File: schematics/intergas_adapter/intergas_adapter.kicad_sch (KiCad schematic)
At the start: 12 parts, among them J1 RJ45, Q1 BC337, Q2 BC337, U1 4N25, U2 ESP-12E, U3 4N25, U4 HT7533-1-TO92

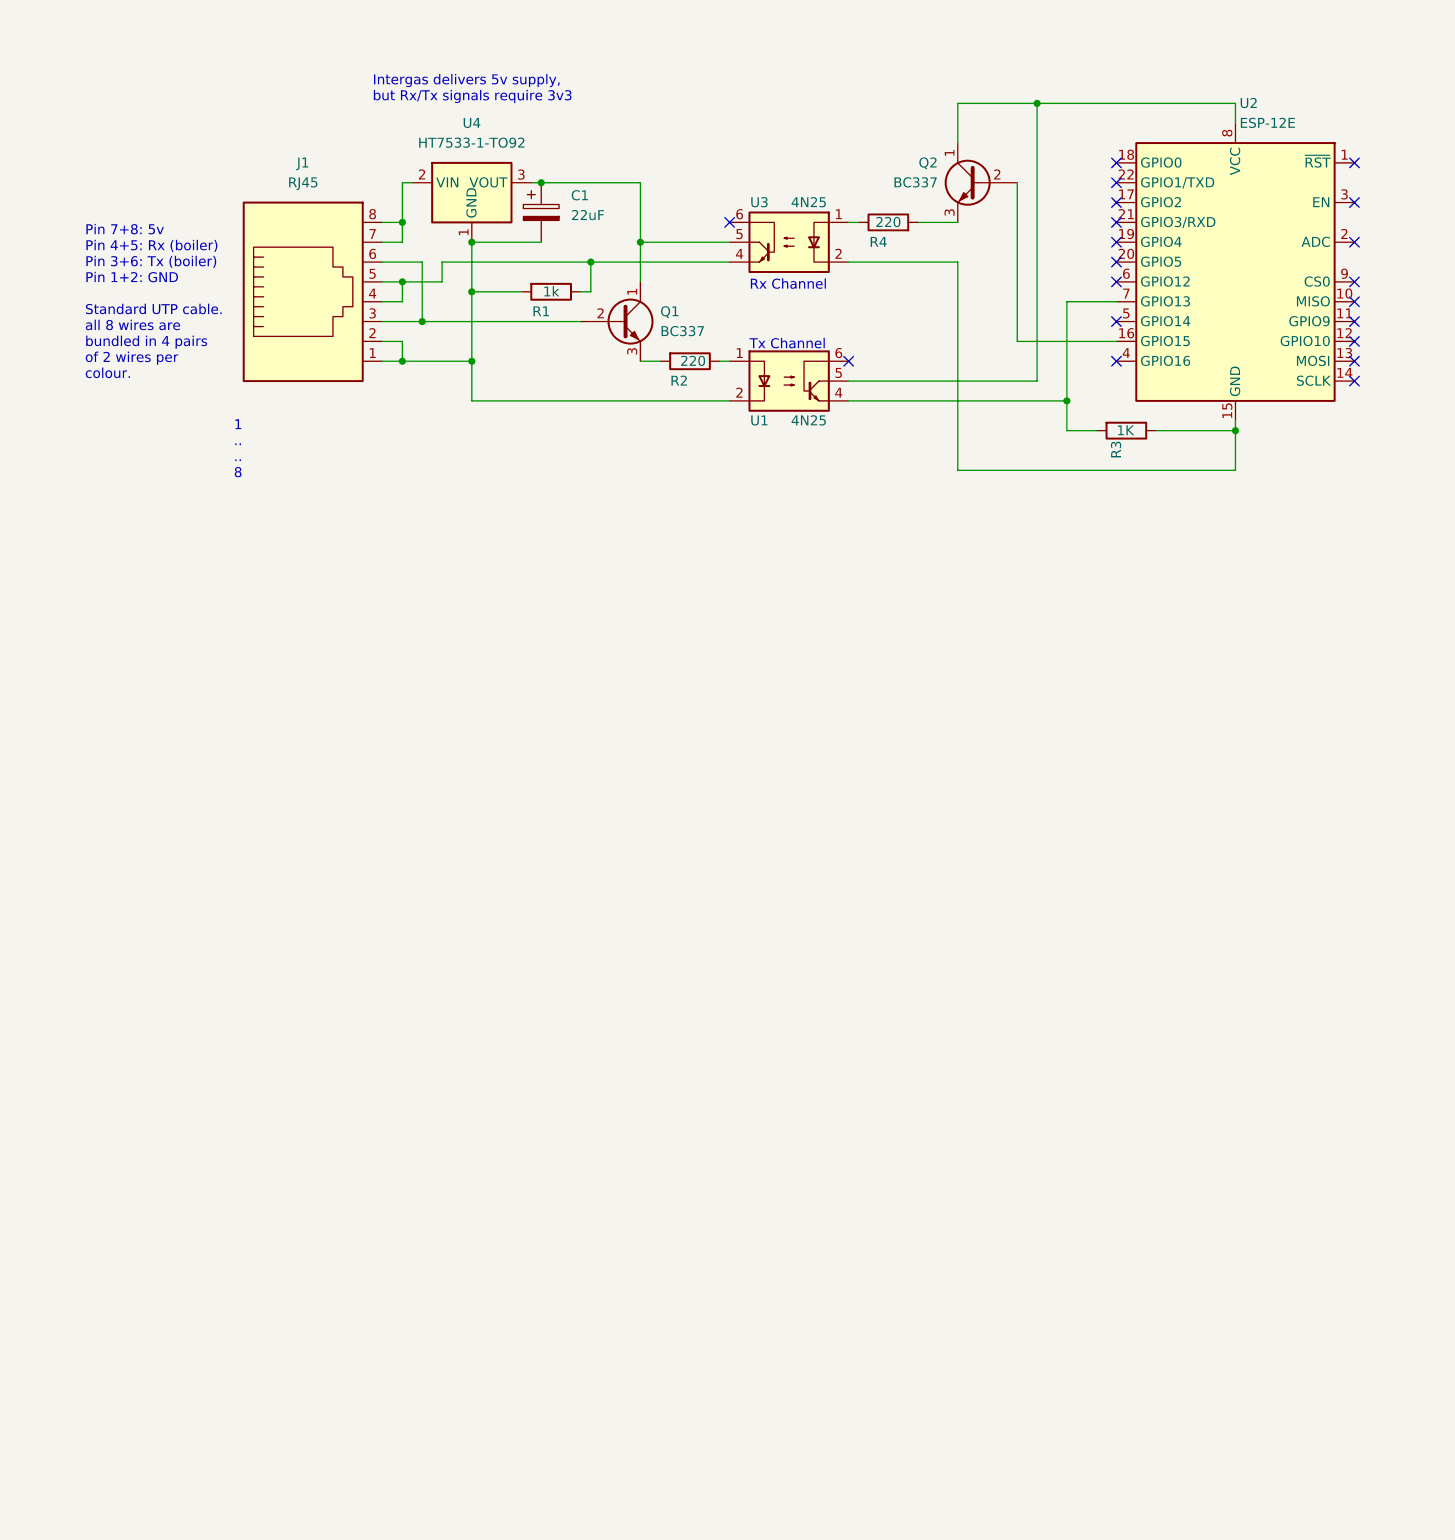
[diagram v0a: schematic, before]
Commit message: Add NodeMCU-ESP32 support
Next to the NodeMCU-ESP8266 we do now support also a
NodeMCU-ESP32 board: https://esphome.io/devices/nodemcu_esp32.html
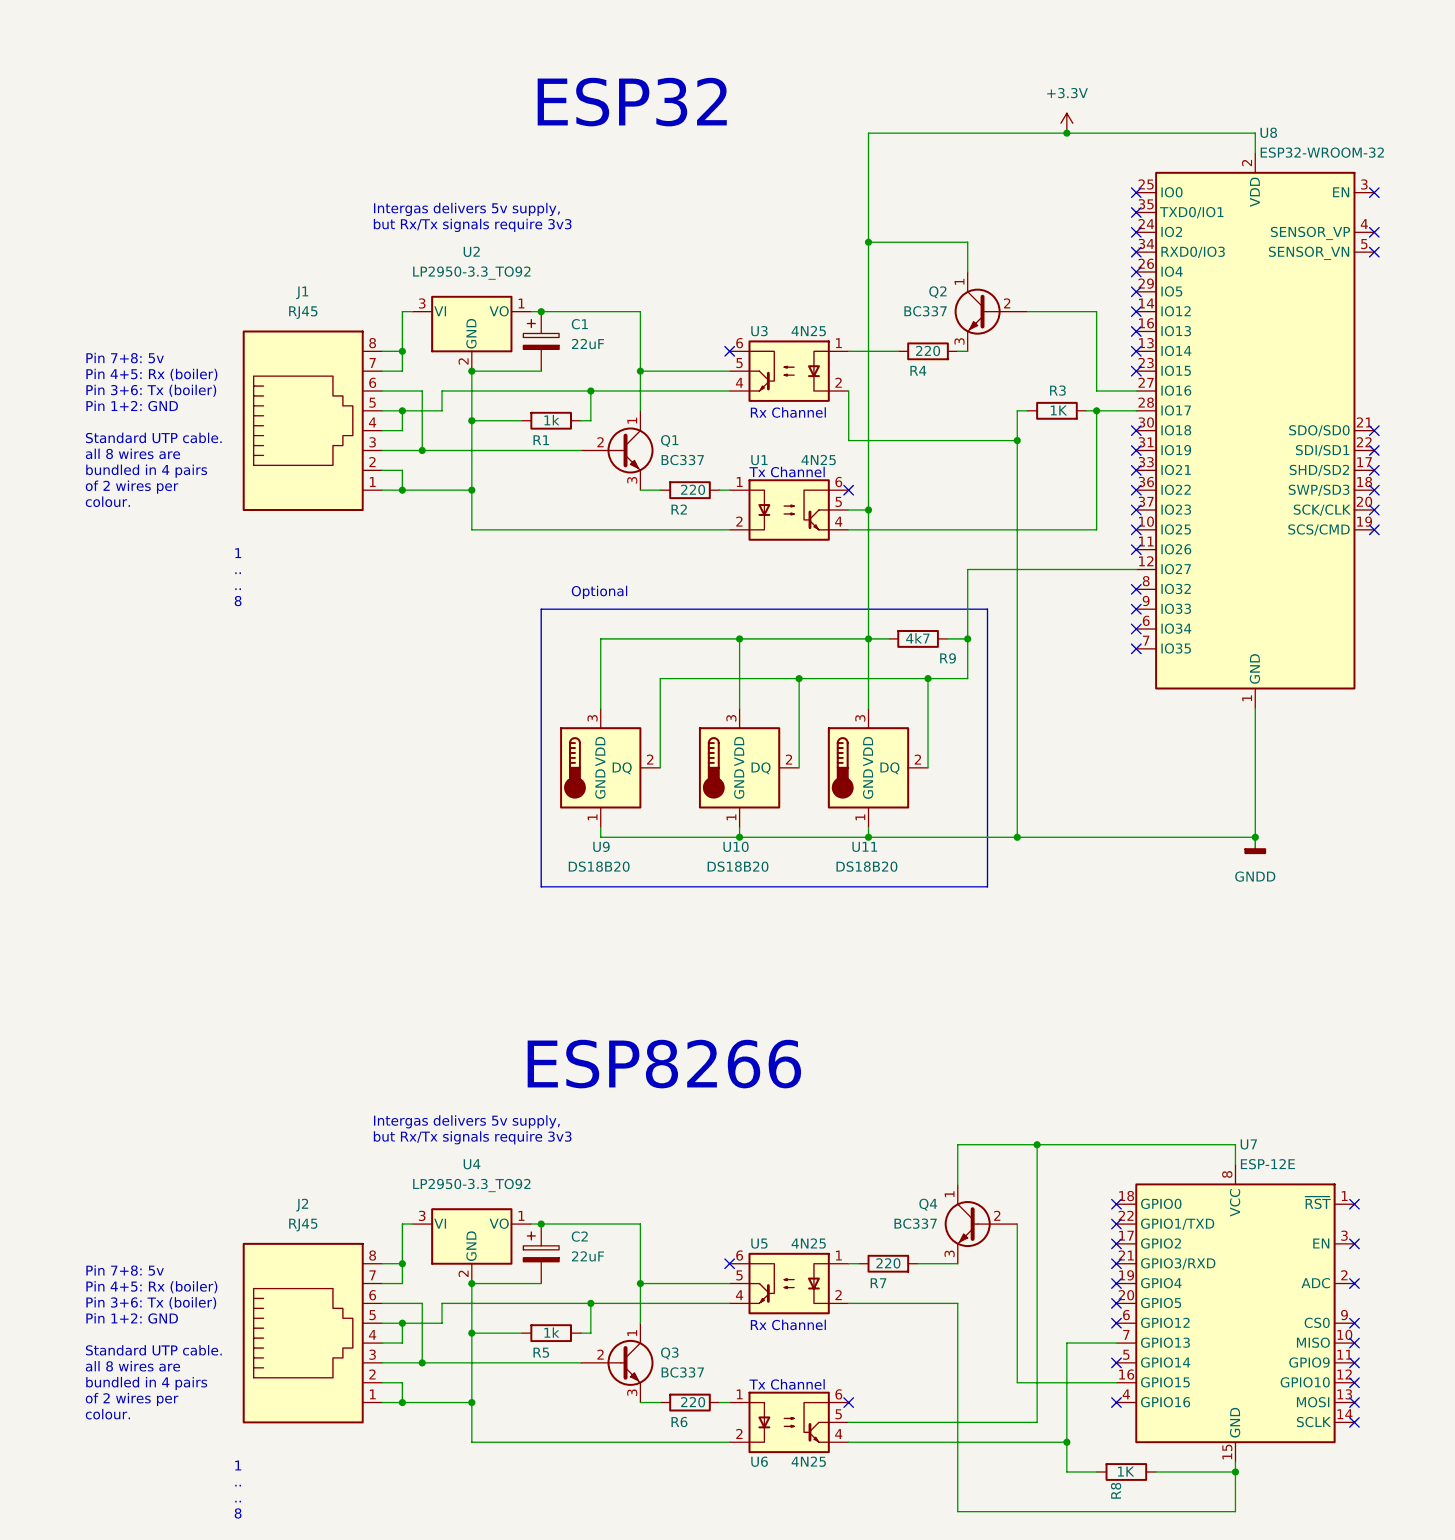
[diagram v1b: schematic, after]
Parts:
- removed U2: ESP-12E, RF_Module:ESP-12E, symbol RF_Module:ESP-12E
- removed U4: HT7533-1-TO92, symbol Regulator_Linear:HT75xx-1-SOT89
- added C2: 22uF, symbol Device:C_Polarized
- added J2: RJ45, symbol Connector:RJ45
- added Q3, Q4: BC337, Package_TO_SOT_THT:TO-92_Inline, symbol Transistor_BJT:BC337
- added R5: 1k, symbol Device:R
- added R6, R7: 220, symbol Device:R
- added R8: 1K, symbol Device:R
- added R9: 4k7, symbol Device:R
- added U10, U11, U9: DS18B20, Package_TO_SOT_THT:TO-92_Inline, symbol Sensor_Temperature:DS18B20
- added U2, U4: LP2950-3.3_TO92, Package_TO_SOT_THT:TO-92_Inline, symbol Regulator_Linear:LP2950-3.3_TO92
- added U5, U6: 4N25, Package_DIP:DIP-6_W7.62mm, symbol Isolator:4N25
- added U7: ESP-12E, RF_Module:ESP-12E, symbol RF_Module:ESP-12E
- added U8: ESP32-WROOM-32, RF_Module:ESP32-WROOM-32, symbol RF_Module:ESP32-WROOM-32
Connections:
- net +3V3: now reaches Q2.1 (C), U1.5
- net +3V3: now also R9.2, U10.3 (VDD), U11.3 (VDD), U8.2 (VDD), U9.3 (VDD)
- net at Q2.2 (B): now also U8.27 (IO16)
- net GNDD: now reaches R3.1, U3.2
- net GNDD: now also U10.1 (GND), U11.1 (GND), U8.1 (GND), U8.15 (GND), U8.38 (GND), U8.39 (GND), U9.1 (GND)
- net at R3.2, U1.4: now also U8.28 (IO17)
- net at C1.2, J1.1, J1.2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: now also U2.2 (GND)
- net at J1.7, J1.8: now also U2.3 (VI)
- net at C1.1, Q1.1 (C), U3.5: now also U2.1 (VO)
- new net: R6.1, U6.1
- new net: C2.2, J2.1, J2.2, R5.2, U4.2 (GND), U6.2
- new net: R8.2, U6.4, U7.7 (GPIO13)
- new net: Q4.1 (C), U6.5, U7.8 (VCC)
- new net: R9.1, U10.2 (DQ), U11.2 (DQ), U8.12 (IO27), U9.2 (DQ)
- new net: R8.1, U5.2, U7.15 (GND)
- new net: Q3.3 (E), R6.2
- new net: C2.1, Q3.1 (C), U4.1 (VO), U5.5
- new net: R7.1, U5.1
- new net: J2.4, J2.5, R5.1, U5.4
- new net: Q4.2 (B), U7.16 (GPIO15)
- new net: Q4.3 (E), R7.2
- new net: J2.3, J2.6, Q3.2 (B)
- new net: J2.7, J2.8, U4.3 (VI)
- no-connect marks 20 -> 52
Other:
- note added: "ESP32"
- note added: "ESP8266"
- note added: "Optional"
- moved on the sheet: C1, J1, Q1, Q2, R1, R2, R4, U3

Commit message: Drop esp8266 support
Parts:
- removed C2: 22uF, symbol Device:C_Polarized
- removed J2: RJ45, symbol Connector:RJ45
- removed Q3, Q4: BC337, Package_TO_SOT_THT:TO-92_Inline, symbol Transistor_BJT:BC337
- removed R5: 1k, symbol Device:R
- removed R6, R7: 220, symbol Device:R
- removed R8: 1K, symbol Device:R
- removed U4: LP2950-3.3_TO92, Package_TO_SOT_THT:TO-92_Inline, symbol Regulator_Linear:LP2950-3.3_TO92
- removed U5, U6: 4N25, Package_DIP:DIP-6_W7.62mm, symbol Isolator:4N25
- removed U7: ESP-12E, RF_Module:ESP-12E, symbol RF_Module:ESP-12E
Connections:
- net at Q2.2 (B): now also U8.28 (IO17); no longer U8.27 (IO16)
- net at R3.2, U1.4: now also U8.27 (IO16); no longer U8.28 (IO17)
- no-connect marks 52 -> 32
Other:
- note removed: "ESP8266"
- moved on the sheet: C1, J1, Q1, Q2, R1, R2, R3, R4, R9, U1, U10, U11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
